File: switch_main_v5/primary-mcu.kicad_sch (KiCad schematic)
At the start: 50 parts, among them Q801 DMP21D0UFB-7B, U801 FM25CL64B-DG, U802 STM32H573IIKxQ, Y801 XRCGB25M000F3A16R0, Y802 ECS-.327-7-12QS-TR

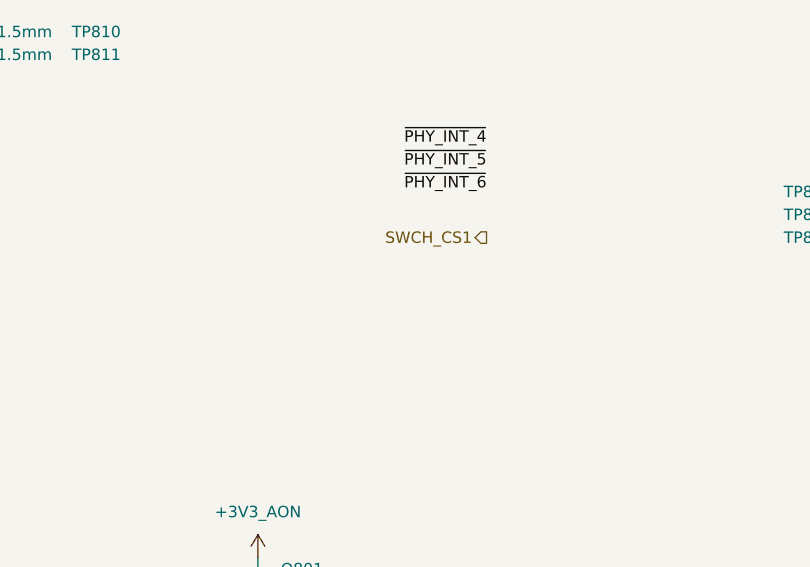
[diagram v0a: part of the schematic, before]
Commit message: MDIO multiplexing
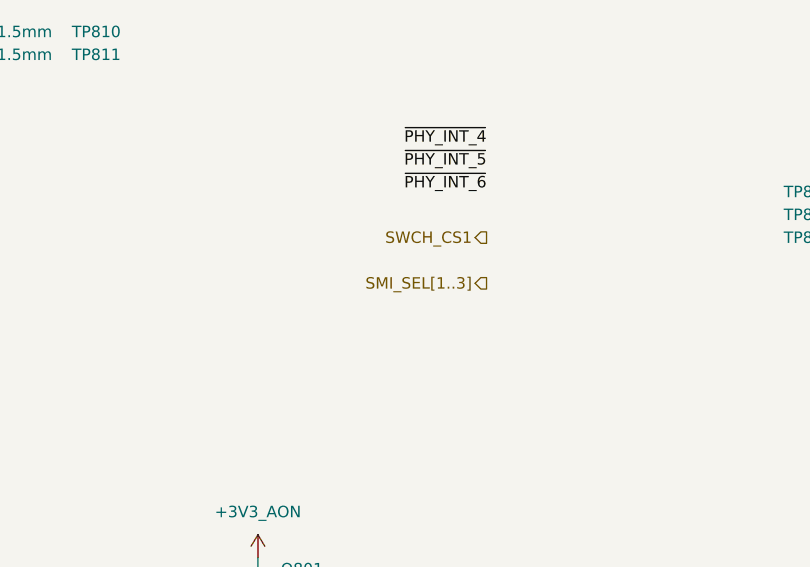
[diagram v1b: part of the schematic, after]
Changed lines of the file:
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@@
 	(title_block
 		(title "Primary MCU")
-		(date "2025-06-30")
 		(comment 3 "It also runs algorithms like MSTP.")
 		(comment 4 "This microcontroller is responsible for managing the ethernet switch and PHYs.")
@@
 		(effects
 			(font
+				(size 1.27 1.27)
+			)
+			(justify right)
+		)
+	)
+	(hierarchical_label "SMI_SEL[1..3]"
+		(shape output)
+		(at 132.08 96.52 180)
+		(effects
+			(font

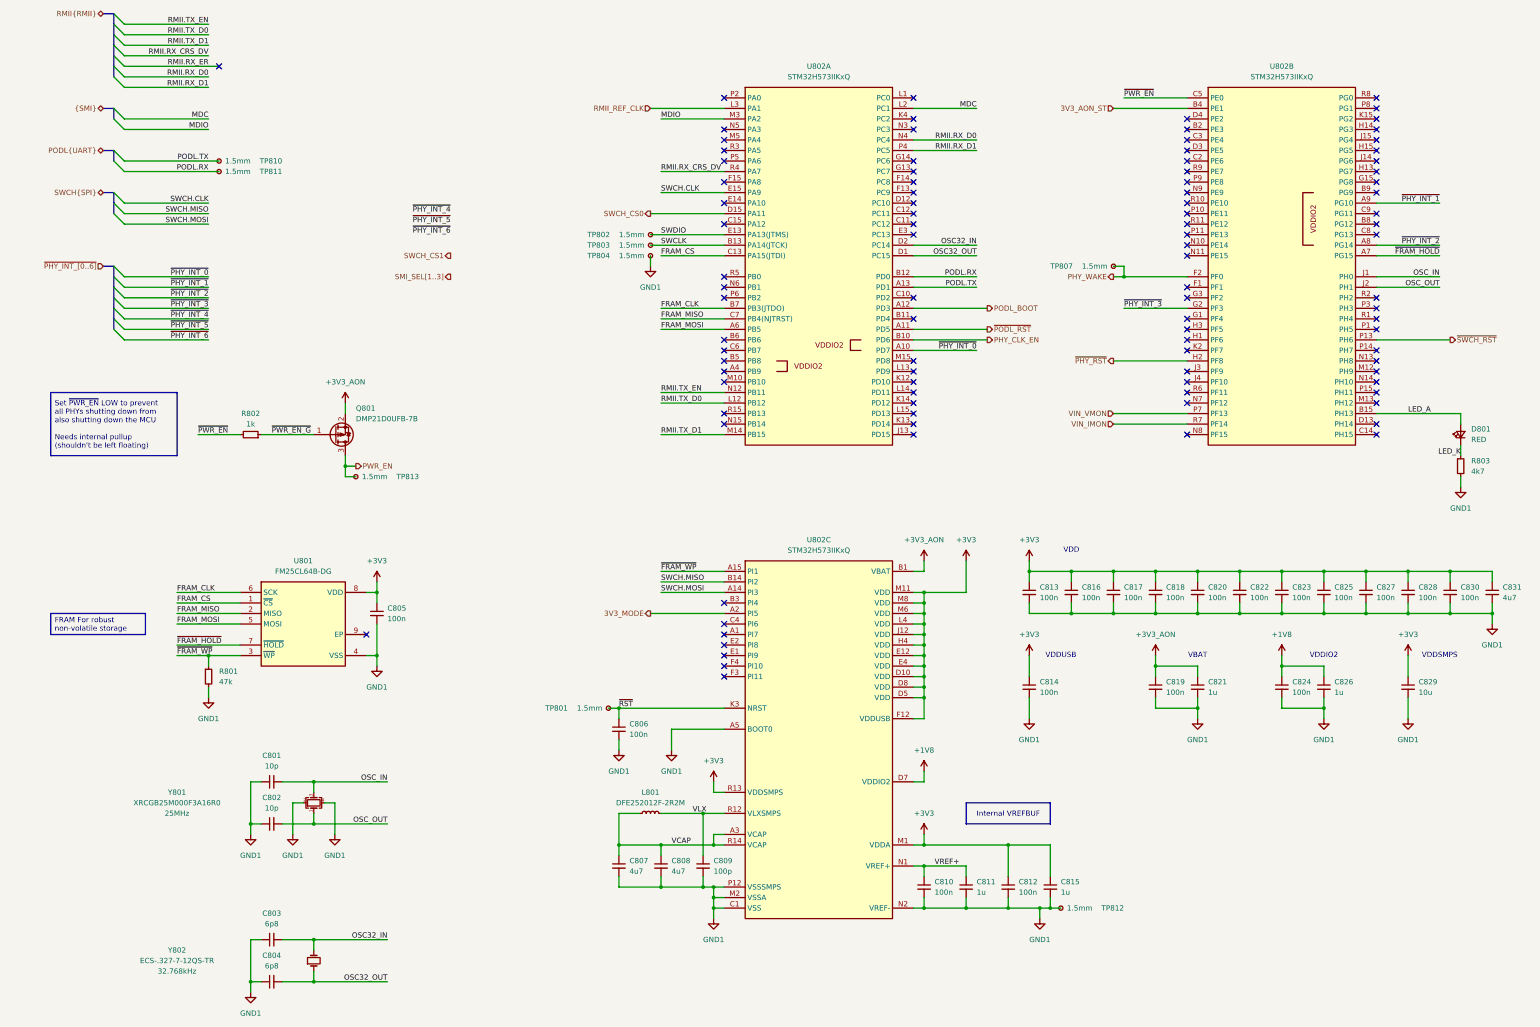
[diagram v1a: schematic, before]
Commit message: Updated 1v0_buck_converter feedback resistors
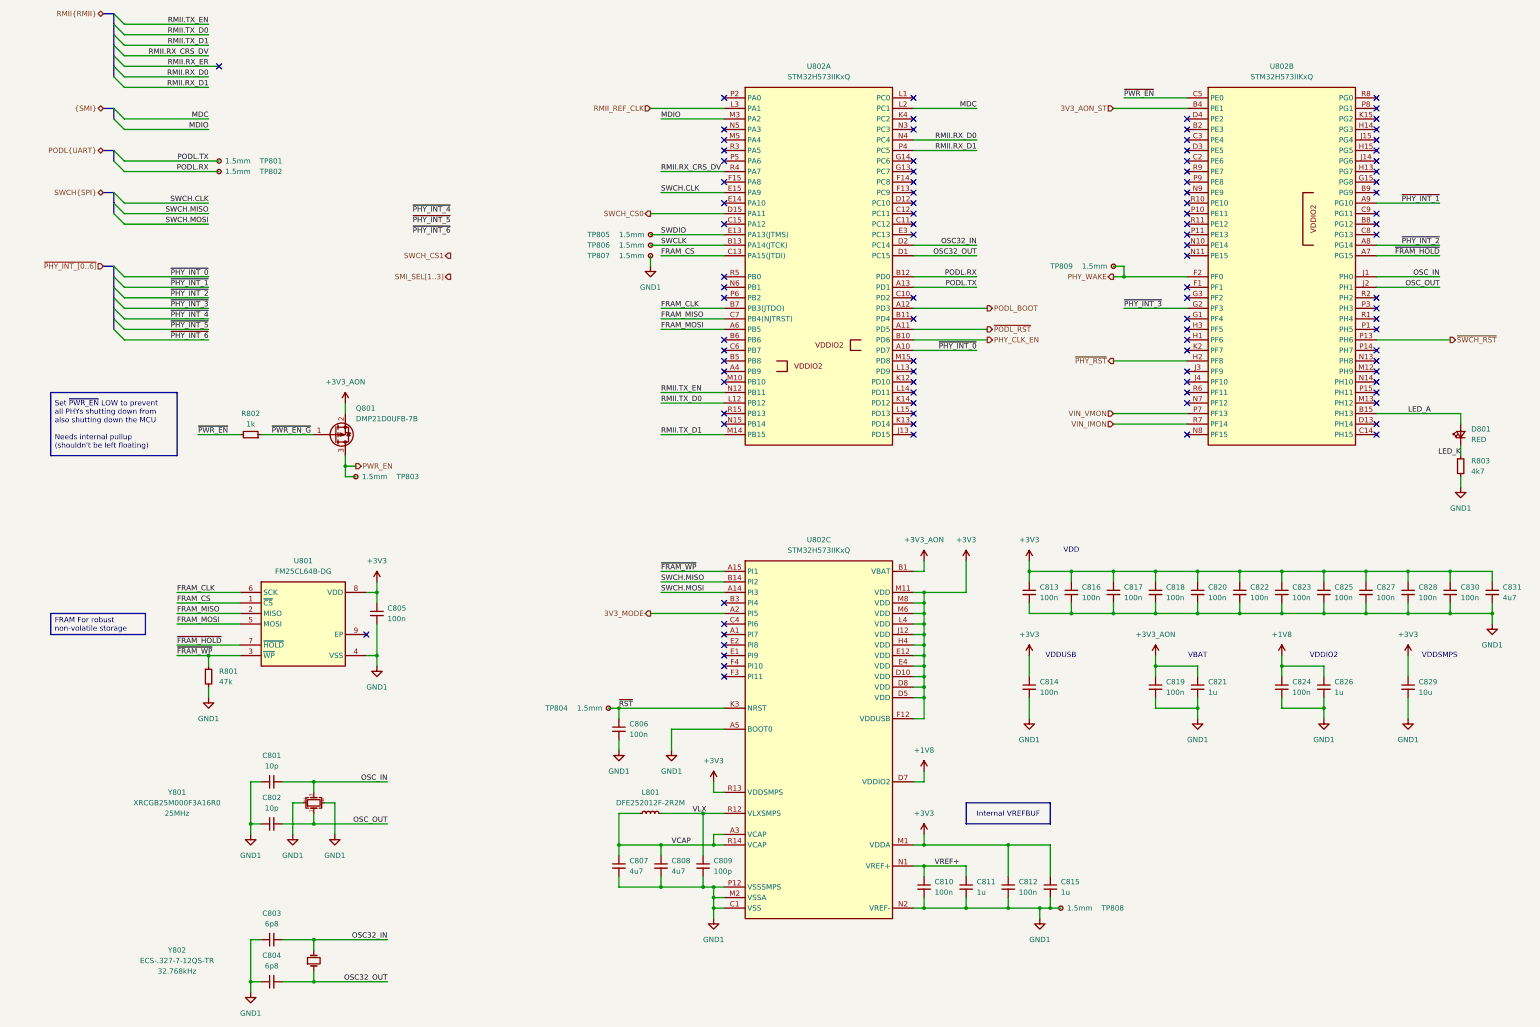
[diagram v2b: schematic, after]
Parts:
- renumbered TP810 to TP801, TP811 to TP802, TP813 to TP803, TP801 to TP804, TP802 to TP805, TP803 to TP806, TP804 to TP807, TP812 to TP808, TP807 to TP809
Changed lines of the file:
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@@
 		(dnp no)
 		(fields_autoplaced yes)
-		(property "Reference" "#PWR0823"
+		(property "Reference" "#PWR0824"
 			(at 332.74 191.77 0)
 			(effects
@@
 			(project "switch_main_v4"
 				(path "/a5e57332-4284-4d3c-ab3c-13bc0ddb29b6/cc240678-80bc-4d6d-9d13-1541d9f89447"
-					(reference "#PWR0823")
+					(reference "#PWR0824")
 					(unit 1)
 				)
@@
 		(on_board yes)
 		(dnp no)
-		(property "Reference" "TP811"
+		(property "Reference" "TP802"
 			(at 91.44 71.12 0)
 			(effects
@@
 			(project "switch_main_v4"
 				(path "/a5e57332-4284-4d3c-ab3c-13bc0ddb29b6/cc240678-80bc-4d6d-9d13-1541d9f89447"
-					(reference "TP811")
+					(reference "TP802")
 					(unit 1)
 				)
@@
 		(dnp no)
 		(fields_autoplaced yes)
-		(property "Reference" "#PWR0817"
+		(property "Reference" "#PWR0818"
 			(at 271.78 168.91 0)
 			(effects
@@
 			(project "switch_main_v4"
 				(path "/a5e57332-4284-4d3c-ab3c-13bc0ddb29b6/cc240678-80bc-4d6d-9d13-1541d9f89447"
-					(reference "#PWR0817")
+					(reference "#PWR0818")
 					(unit 1)
 				)
@@
 		(dnp no)
 		(fields_autoplaced yes)
-		(property "Reference" "#PWR0814"
+		(property "Reference" "#PWR0815"
 			(at 246.38 219.71 0)
 			(effects
@@
 			(project ""
 				(path "/a5e57332-4284-4d3c-ab3c-13bc0ddb29b6/cc240678-80bc-4d6d-9d13-1541d9f89447"
-					(reference "#PWR0814")
+					(reference "#PWR0815")
 					(unit 1)
 				)
@@
 		(dnp no)
 		(fields_autoplaced yes)
-		(property "Reference" "#PWR0816"
+		(property "Reference" "#PWR0817"
 			(at 256.54 168.91 0)
 			(effects
@@
 			(project "switch_main_v4"
 				(path "/a5e57332-4284-4d3c-ab3c-13bc0ddb29b6/cc240678-80bc-4d6d-9d13-1541d9f89447"
-					(reference "#PWR0816")
+					(reference "#PWR0817")
 					(unit 1)
 				)
@@
 		(on_board yes)
 		(dnp no)
-		(property "Reference" "TP804"
+		(property "Reference" "TP807"
 			(at 165.1 91.44 0)
 			(effects
@@
 			(project "switch_main_v4"
 				(path "/a5e57332-4284-4d3c-ab3c-13bc0ddb29b6/cc240678-80bc-4d6d-9d13-1541d9f89447"
-					(reference "TP804")
+					(reference "TP807")
 					(unit 1)
 				)
@@
 		(dnp no)
 		(fields_autoplaced yes)
-		(property "Reference" "#PWR0822"
+		(property "Reference" "#PWR0823"
 			(at 312.42 209.55 0)
 			(effects
@@
 			(project "switch_main_v4"
 				(path "/a5e57332-4284-4d3c-ab3c-13bc0ddb29b6/cc240678-80bc-4d6d-9d13-1541d9f89447"
-					(reference "#PWR0822")
+					(reference "#PWR0823")
 					(unit 1)
 				)
@@
 		(on_board yes)
 		(dnp no)
-		(property "Reference" "TP803"
+		(property "Reference" "TP806"
 			(at 165.1 88.9 0)
 			(effects
@@
 			(project "switch_main_v4"
 				(path "/a5e57332-4284-4d3c-ab3c-13bc0ddb29b6/cc240678-80bc-4d6d-9d13-1541d9f89447"
-					(reference "TP803")
+					(reference "TP806")
 					(unit 1)
 				)
@@
 		(on_board yes)
 		(dnp no)
-		(property "Reference" "TP813"
+		(property "Reference" "TP803"
 			(at 124.46 144.78 0)
 			(effects
@@
 			(project "switch_main_v4"
 				(path "/a5e57332-4284-4d3c-ab3c-13bc0ddb29b6/cc240678-80bc-4d6d-9d13-1541d9f89447"
-					(reference "TP813")
+					(reference "TP803")
 					(unit 1)
 				)
@@
 		(on_board yes)
 		(dnp no)
-		(property "Reference" "TP802"
+		(property "Reference" "TP805"
 			(at 165.1 86.36 0)
 			(effects
@@
 			(project "switch_main_v4"
 				(path "/a5e57332-4284-4d3c-ab3c-13bc0ddb29b6/cc240678-80bc-4d6d-9d13-1541d9f89447"
-					(reference "TP802")
+					(reference "TP805")
 					(unit 1)
 				)
@@
 		(dnp no)
 		(fields_autoplaced yes)
-		(property "Reference" "#PWR0813"
+		(property "Reference" "#PWR0814"
 			(at 246.38 168.91 0)
 			(effects
@@
 			(project "switch_main_v4"
 				(path "/a5e57332-4284-4d3c-ab3c-13bc0ddb29b6/cc240678-80bc-4d6d-9d13-1541d9f89447"
-					(reference "#PWR0813")
+					(reference "#PWR0814")
 					(unit 1)
 				)
@@
 		(on_board yes)
 		(dnp no)
-		(property "Reference" "TP810"
+		(property "Reference" "TP801"
 			(at 91.44 68.58 0)
 			(effects
@@
 			(project "switch_main_v4"
 				(path "/a5e57332-4284-4d3c-ab3c-13bc0ddb29b6/cc240678-80bc-4d6d-9d13-1541d9f89447"
-					(reference "TP810")
+					(reference "TP801")
 					(unit 1)
 				)
@@
 		(dnp no)
 		(fields_autoplaced yes)
-		(property "Reference" "#PWR0305"
+		(property "Reference" "#PWR0810"
 			(at 180.34 100.33 0)
 			(effects
@@
 			(project "switch_main_v4"
 				(path "/a5e57332-4284-4d3c-ab3c-13bc0ddb29b6/cc240678-80bc-4d6d-9d13-1541d9f89447"
-					(reference "#PWR0305")
+					(reference "#PWR0810")
 					(unit 1)
 				)
@@
 		(on_board yes)
 		(dnp no)
-		(property "Reference" "TP807"
+		(property "Reference" "TP809"
 			(at 276.86 93.98 0)
 			(effects
@@
 			(project "switch_main_v4"
 				(path "/a5e57332-4284-4d3c-ab3c-13bc0ddb29b6/cc240678-80bc-4d6d-9d13-1541d9f89447"
-					(reference "TP807")
+					(reference "TP809")
 					(unit 1)
 				)
@@
 		(dnp no)
 		(fields_autoplaced yes)
-		(property "Reference" "#PWR0827"
+		(property "Reference" "#PWR0829"
 			(at 383.54 186.69 0)
 			(effects
@@
 			(project "switch_main_v4"
 				(path "/a5e57332-4284-4d3c-ab3c-13bc0ddb29b6/cc240678-80bc-4d6d-9d13-1541d9f89447"
-					(reference "#PWR0827")
+					(reference "#PWR0829")
 					(unit 1)
 				)
@@
 		(dnp no)
 		(fields_autoplaced yes)
-		(property "Reference" "#PWR0812"
+		(property "Reference" "#PWR0813"
 			(at 195.58 257.81 0)
 			(effects
@@
 			(project "switch_main_v4"
 				(path "/a5e57332-4284-4d3c-ab3c-13bc0ddb29b6/cc240678-80bc-4d6d-9d13-1541d9f89447"
-					(reference "#PWR0812")
+					(reference "#PWR0813")
 					(unit 1)
 				)
@@
 		(dnp no)
 		(fields_autoplaced yes)
-		(property "Reference" "#PWR0818"
+		(property "Reference" "#PWR0819"
 			(at 271.78 191.77 0)
 			(effects
@@
 			(project "switch_main_v4"
 				(path "/a5e57332-4284-4d3c-ab3c-13bc0ddb29b6/cc240678-80bc-4d6d-9d13-1541d9f89447"
-					(reference "#PWR0818")
+					(reference "#PWR0819")
 					(unit 1)
 				)
@@
 		(dnp no)
 		(fields_autoplaced yes)
-		(property "Reference" "#PWR0826"
+		(property "Reference" "#PWR0827"
 			(at 363.22 209.55 0)
 			(effects
@@
 			(project "switch_main_v4"
 				(path "/a5e57332-4284-4d3c-ab3c-13bc0ddb29b6/cc240678-80bc-4d6d-9d13-1541d9f89447"
-					(reference "#PWR0826")
+					(reference "#PWR0827")
 					(unit 1)
 				)
@@
 		(dnp no)
 		(fields_autoplaced yes)
-		(property "Reference" "#PWR0824"
+		(property "Reference" "#PWR0825"
 			(at 342.9 209.55 0)
 			(effects
@@
 			(project "switch_main_v4"
 				(path "/a5e57332-4284-4d3c-ab3c-13bc0ddb29b6/cc240678-80bc-4d6d-9d13-1541d9f89447"
-					(reference "#PWR0824")
+					(reference "#PWR0825")
 					(unit 1)
 				)
@@
 		(on_board yes)
 		(dnp no)
-		(property "Reference" "TP801"
+		(property "Reference" "TP804"
 			(at 154.94 200.66 0)
 			(effects
@@
 			(project "switch_main_v4"
 				(path "/a5e57332-4284-4d3c-ab3c-13bc0ddb29b6/cc240678-80bc-4d6d-9d13-1541d9f89447"
-					(reference "TP801")
+					(reference "TP804")
 					(unit 1)
 				)
@@
 		(dnp no)
 		(fields_autoplaced yes)
-		(property "Reference" "#PWR0810"
+		(property "Reference" "#PWR0811"
 			(at 185.42 217.17 0)
 			(effects
@@
 			(project "switch_main_v4"
 				(path "/a5e57332-4284-4d3c-ab3c-13bc0ddb29b6/cc240678-80bc-4d6d-9d13-1541d9f89447"
-					(reference "#PWR0810")
+					(reference "#PWR0811")
 					(unit 1)
 				)
@@
 		(on_board yes)
 		(dnp no)
-		(property "Reference" "TP812"
+		(property "Reference" "TP808"
 			(at 294.64 248.92 0)
 			(effects
@@
 			(project "switch_main_v4"
 				(path "/a5e57332-4284-4d3c-ab3c-13bc0ddb29b6/cc240678-80bc-4d6d-9d13-1541d9f89447"
-					(reference "TP812")
+					(reference "TP808")
 					(unit 1)
 				)
@@
 		(dnp no)
 		(fields_autoplaced yes)
-		(property "Reference" "#PWR0815"
+		(property "Reference" "#PWR0816"
 			(at 246.38 234.95 0)
 			(effects
@@
 			(project "switch_main_v4"
 				(path "/a5e57332-4284-4d3c-ab3c-13bc0ddb29b6/cc240678-80bc-4d6d-9d13-1541d9f89447"
-					(reference "#PWR0815")
+					(reference "#PWR0816")
 					(unit 1)
 				)
@@
 		(dnp no)
 		(fields_autoplaced yes)
-		(property "Reference" "#PWR0811"
+		(property "Reference" "#PWR0812"
 			(at 195.58 222.25 0)
 			(effects
@@
 			(project "switch_main_v4"
 				(path "/a5e57332-4284-4d3c-ab3c-13bc0ddb29b6/cc240678-80bc-4d6d-9d13-1541d9f89447"
-					(reference "#PWR0811")
+					(reference "#PWR0812")
 					(unit 1)
 				)
@@
 		(dnp no)
 		(fields_autoplaced yes)
-		(property "Reference" "#PWR0825"
+		(property "Reference" "#PWR0826"
 			(at 363.22 191.77 0)
 			(effects
@@
 			(project "switch_main_v4"
 				(path "/a5e57332-4284-4d3c-ab3c-13bc0ddb29b6/cc240678-80bc-4d6d-9d13-1541d9f89447"
-					(reference "#PWR0825")
+					(reference "#PWR0826")
 					(unit 1)
 				)
@@
 		(dnp no)
 		(fields_autoplaced yes)
-		(property "Reference" "#PWR0821"
+		(property "Reference" "#PWR0822"
 			(at 302.26 191.77 0)
 			(effects
@@
 			(project "switch_main_v4"
 				(path "/a5e57332-4284-4d3c-ab3c-13bc0ddb29b6/cc240678-80bc-4d6d-9d13-1541d9f89447"
-					(reference "#PWR0821")
+					(reference "#PWR0822")
 					(unit 1)
 				)
@@
 		(dnp no)
 		(fields_autoplaced yes)
-		(property "Reference" "#PWR0819"
+		(property "Reference" "#PWR0820"
 			(at 271.78 209.55 0)
 			(effects
@@
 			(project "switch_main_v4"
 				(path "/a5e57332-4284-4d3c-ab3c-13bc0ddb29b6/cc240678-80bc-4d6d-9d13-1541d9f89447"
-					(reference "#PWR0819")
+					(reference "#PWR0820")
 					(unit 1)
 				)
@@
 		(dnp no)
 		(fields_autoplaced yes)
-		(property "Reference" "#PWR0820"
+		(property "Reference" "#PWR0821"
 			(at 274.32 257.81 0)
 			(effects
@@
 			(project "switch_main_v4"
 				(path "/a5e57332-4284-4d3c-ab3c-13bc0ddb29b6/cc240678-80bc-4d6d-9d13-1541d9f89447"
-					(reference "#PWR0820")
+					(reference "#PWR0821")
 					(unit 1)
 				)

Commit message: Changed main 3V3 regulator to 3A, added switch 2 crystal & other changes
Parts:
- L801: symbol Device:L_Small -> PWR-IND:DFE252012F-2R2M
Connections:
- net VCAP: now also L801.2; no longer L801.1
- net VLX: now also L801.1; no longer L801.2
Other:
- moved on the sheet: L801
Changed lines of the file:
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@@
 	)
 	(symbol
-		(lib_id "Device:L_Small")
-		(at 180.34 226.06 90)
+		(lib_id "PWR-IND:DFE252012F-2R2M")
+		(at 180.34 226.06 270)
+		(mirror x)
 		(unit 1)
 		(exclude_from_sim no)
@@
 		(on_board yes)
 		(dnp no)
-		(fields_autoplaced yes)
 		(property "Reference" "L801"
 			(at 180.34 220.98 90)
@@
 			)
 		)
-		(property "Datasheet" "~"
+		(property "Datasheet" "https://www.mouser.co.uk/datasheet/3/76/2/J_E_TE243A_0017.pdf"
 			(at 180.34 226.06 0)
 			(effects
